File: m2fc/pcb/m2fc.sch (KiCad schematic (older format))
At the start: 31 parts

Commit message: rename m2d to m2fc which now incorporates m2p
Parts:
- added C?: 100n, 0603, symbol C
- added U?: MICROSD, symbol MICROSD
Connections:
- net labels added: SD_CD, SD_CLK, SD_CMD, SD_DAT0, SD_DAT1, SD_DAT2, SD_DAT3
- wire segments 137 -> 119
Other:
- note added: "MICRO SD CARD"
- note removed: "TODO\n* SD Card\n* Thermocouple layout\n* Spec gain resistor for strain gauges"

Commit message: update more bits on flight computer..
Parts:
- removed C?: 1n, 0603, symbol C
- removed IC?: APU1205-HF-3, symbol APU1205-HF-3
- removed IC?: STM32F415RG, symbol STM32F415RG
- added C? (x3): 100n, 0603, symbol C
- added C?: 1n, 0603, symbol C
- added IC?: STM32F405VGT, symbol STM32F405VGT
- added IC?: ADP3335, MSOP-8, symbol ADP3335
- added TP? (x7): TESTPAD, symbol TESTPAD
- C?: value 100n -> 10n; Farnell 1759037 -> 2112704
- R?: Farnell 2331727 -> 2116678
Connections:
- net labels added: BARO_CS, BARO_MISO, BARO_MOSI, BARO_SCK, GYRO_DRDY, GYRO_SCL, GYRO_SDA, HG_ACCEL_CS, HG_ACCEL_INT1, HG_ACCEL_INT2, HG_ACCEL_MISO, HG_ACCEL_MOSI, HG_ACCEL_SCK, LED_1, LED_2, LED_3, LED_A, LED_C, LG_ACCEL_CS, LG_ACCEL_INT1, LG_ACCEL_INT2, LG_ACCEL_MISO, LG_ACCEL_MOSI, LG_ACCEL_SCK, MAGNO_DRDY, MAGNO_SCL, MAGNO_SDA, PYRO_1_C, PYRO_1_F, PYRO_2_C, PYRO_2_F, SER_IN_1, SER_IN_2, SER_OUT_1, SER_OUT_2, STRAIN_1, STRAIN_2, STRAIN_3, THERMO_1, THERMO_2
- wire segments 119 -> 174
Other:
- note added: "* SHARE HALF BRIDGE?\n* TEMPERATURE COMP?"
- moved on the sheet: C?, R?, TP?, X?

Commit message: everything... wired... up...
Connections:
- net BARO_CS: now also IC?.88 (PD7)
- net BARO_MISO: now also IC?.90 (PB4)
- net BARO_MOSI: now also IC?.91 (PB5)
- net BARO_SCK: now also IC?.89 (PB3)
- net BAT_MON: now also IC?.26 (PA3)
- net GYRO_DRDY: now also IC?.97 (PE0)
- net GYRO_SCL: now also IC?.95 (PB8)
- net GYRO_SDA: now also IC?.96 (PB9)
- net HG_ACCEL_CS: now also IC?.29 (PA4)
- net HG_ACCEL_INT1: now also IC?.33 (PC4)
- net HG_ACCEL_INT2: now also IC?.34 (PC5)
- net HG_ACCEL_MISO: now also IC?.31 (PA6)
- net HG_ACCEL_MOSI: now also IC?.32 (PA7)
- net HG_ACCEL_SCK: now also IC?.30 (PA5)
- net LED_1: now also IC?.1 (PE2)
- net LED_2: now also IC?.2 (PE3)
- net LED_3: now also IC?.3 (PE4)
- net LED_A: now also IC?.4 (PE5)
- net LED_C: now also IC?.5 (PE6)
- net LG_ACCEL_CS: now also IC?.51 (PB12)
- net LG_ACCEL_INT1: now also IC?.55 (PD8)
- net LG_ACCEL_INT2: now also IC?.56 (PD9)
- net LG_ACCEL_MISO: now also IC?.53 (PB14)
- net LG_ACCEL_MOSI: now also IC?.54 (PB15)
- net LG_ACCEL_SCK: now also IC?.52 (PB13)
- net MAGNO_DRDY: now also IC?.46 (PE15)
- net MAGNO_SCL: now also IC?.47 (PB10)
- net MAGNO_SDA: now also IC?.48 (PB11)
- net PYRO_1_C: now also IC?.39 (PE8)
- net PYRO_1_F: now also IC?.38 (PE7)
- net PYRO_2_C: now also IC?.40 (PE9)
- net PYRO_2_F: now also IC?.41 (PE10)
- net SD_CD: now also IC?.82 (PD1)
- net SD_CLK: now also IC?.80 (PC12)
- net SD_CMD: now also IC?.83 (PD2)
- net SD_DAT0: now also IC?.65 (PC8)
- net SD_DAT1: now also IC?.66 (PC9)
- net SD_DAT2: now also IC?.78 (PC10)
- net SD_DAT3: now also IC?.79 (PC11)
- net SER_IN_1: now also IC?.93 (PB7)
- net SER_IN_2: now also IC?.87 (PD6)
- net SER_OUT_1: now also IC?.92 (PB6)
- net SER_OUT_2: now also IC?.86 (PD5)
- net STRAIN_1: now also IC?.23 (PA0)
- net STRAIN_2: now also IC?.24 (PA1)
- net STRAIN_3: now also IC?.25 (PA2)
- net SWCLK: now also IC?.76 (PA14)
- net SWDIO: now also IC?.72 (PA13)
- net THERMO_1: now also IC?.16 (PC1)
- net THERMO_2: now also IC?.17 (PC2)
- net THERMO_3: now reaches IC?.18 (PC3)
- net GYRO_INT1: now reaches IC?.98 (PE1)
- no-connect marks 2 -> 30
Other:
- note removed: "* SHARE HALF BRIDGE?\n* TEMPERATURE COMP?"

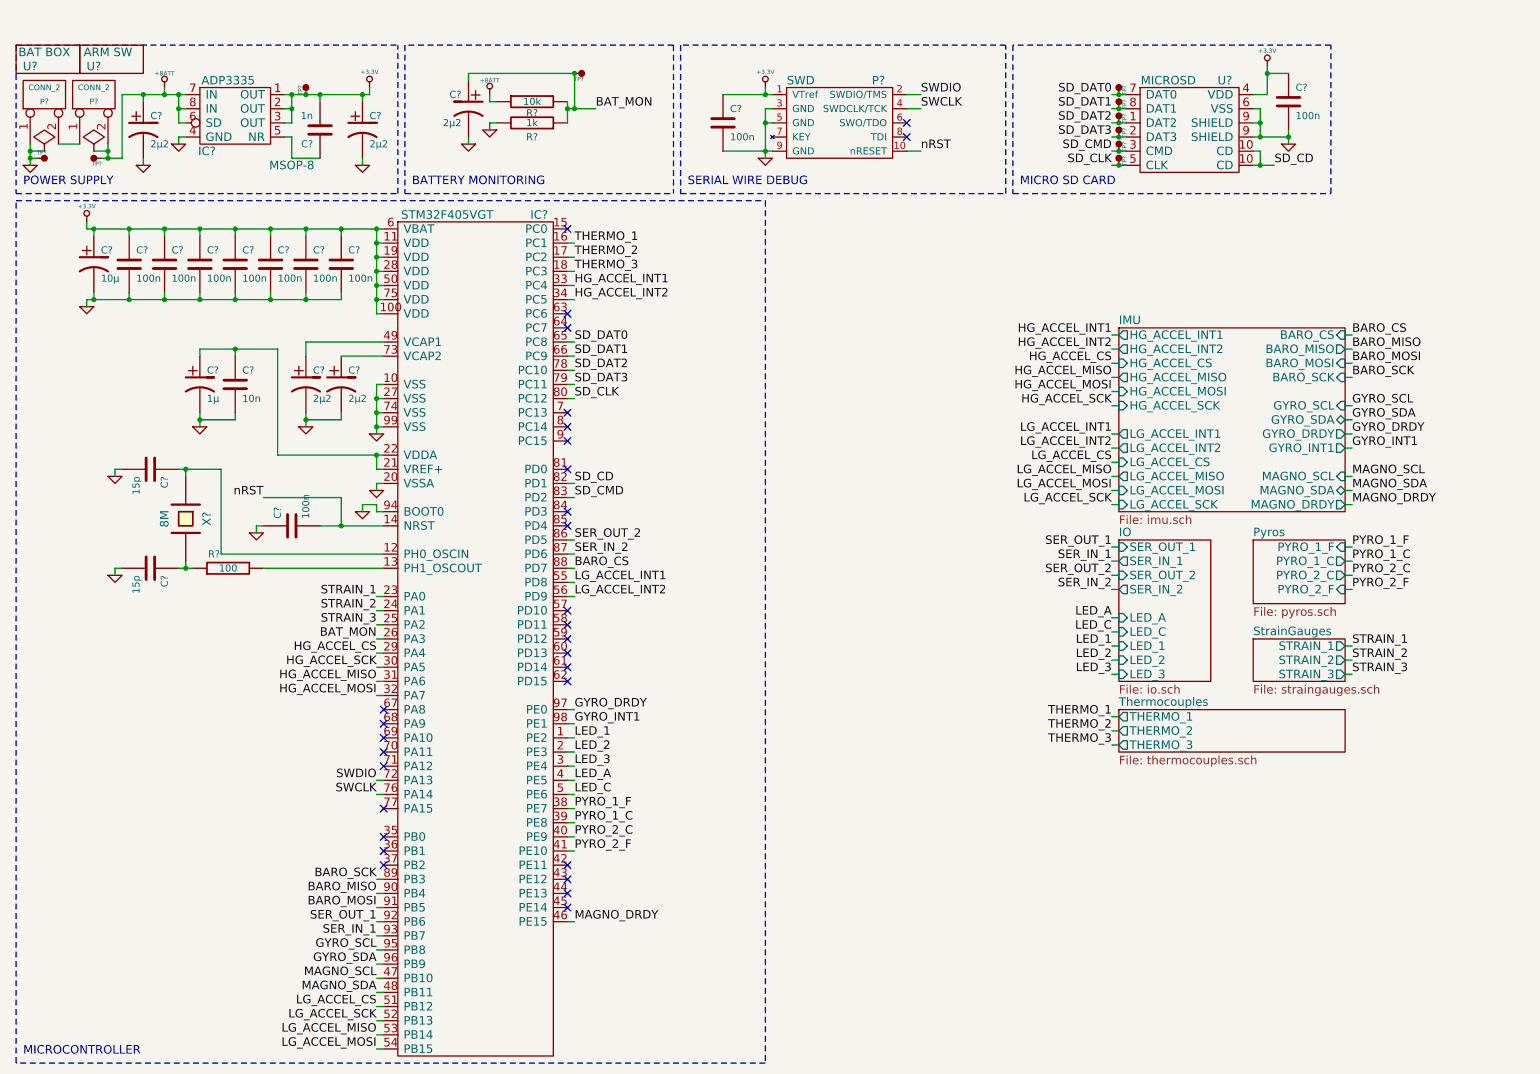
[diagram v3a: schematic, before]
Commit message: fix all the erc errors
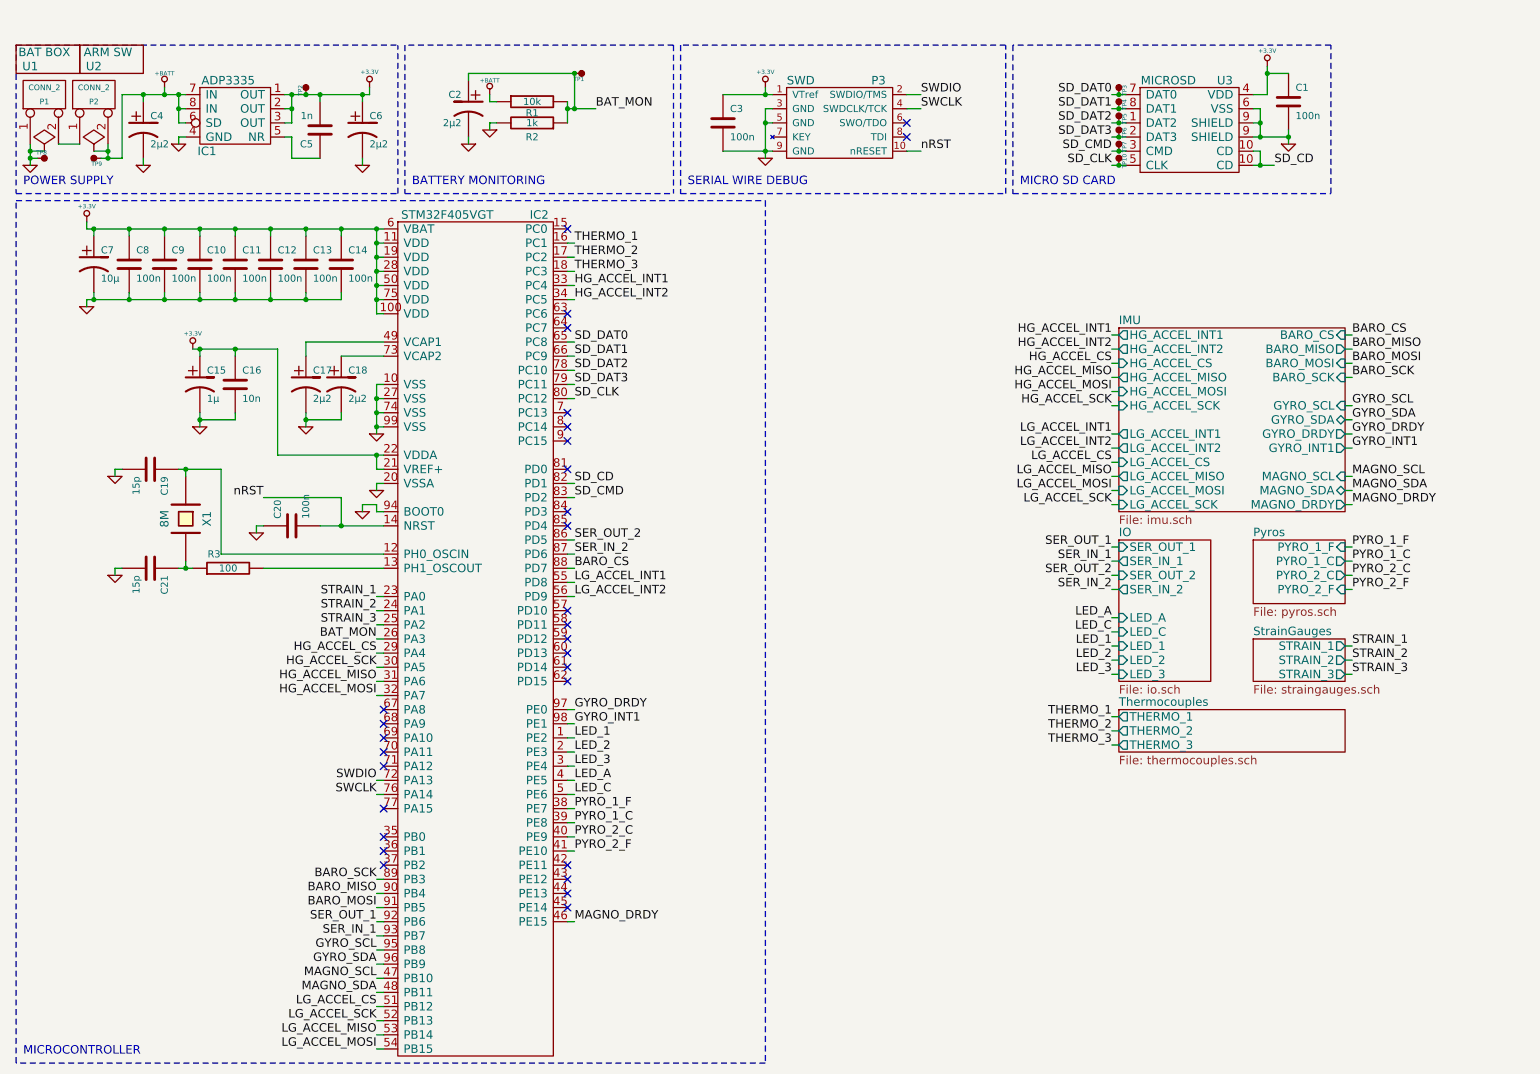
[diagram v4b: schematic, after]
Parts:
- gave numbers to parts that had none: 43
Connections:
- net +3.3V: now also C15.1, C16.1, IC2.21 (VREF+), IC2.22 (VDDA)

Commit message: update m2fc sch with 3rd pyro and SJs
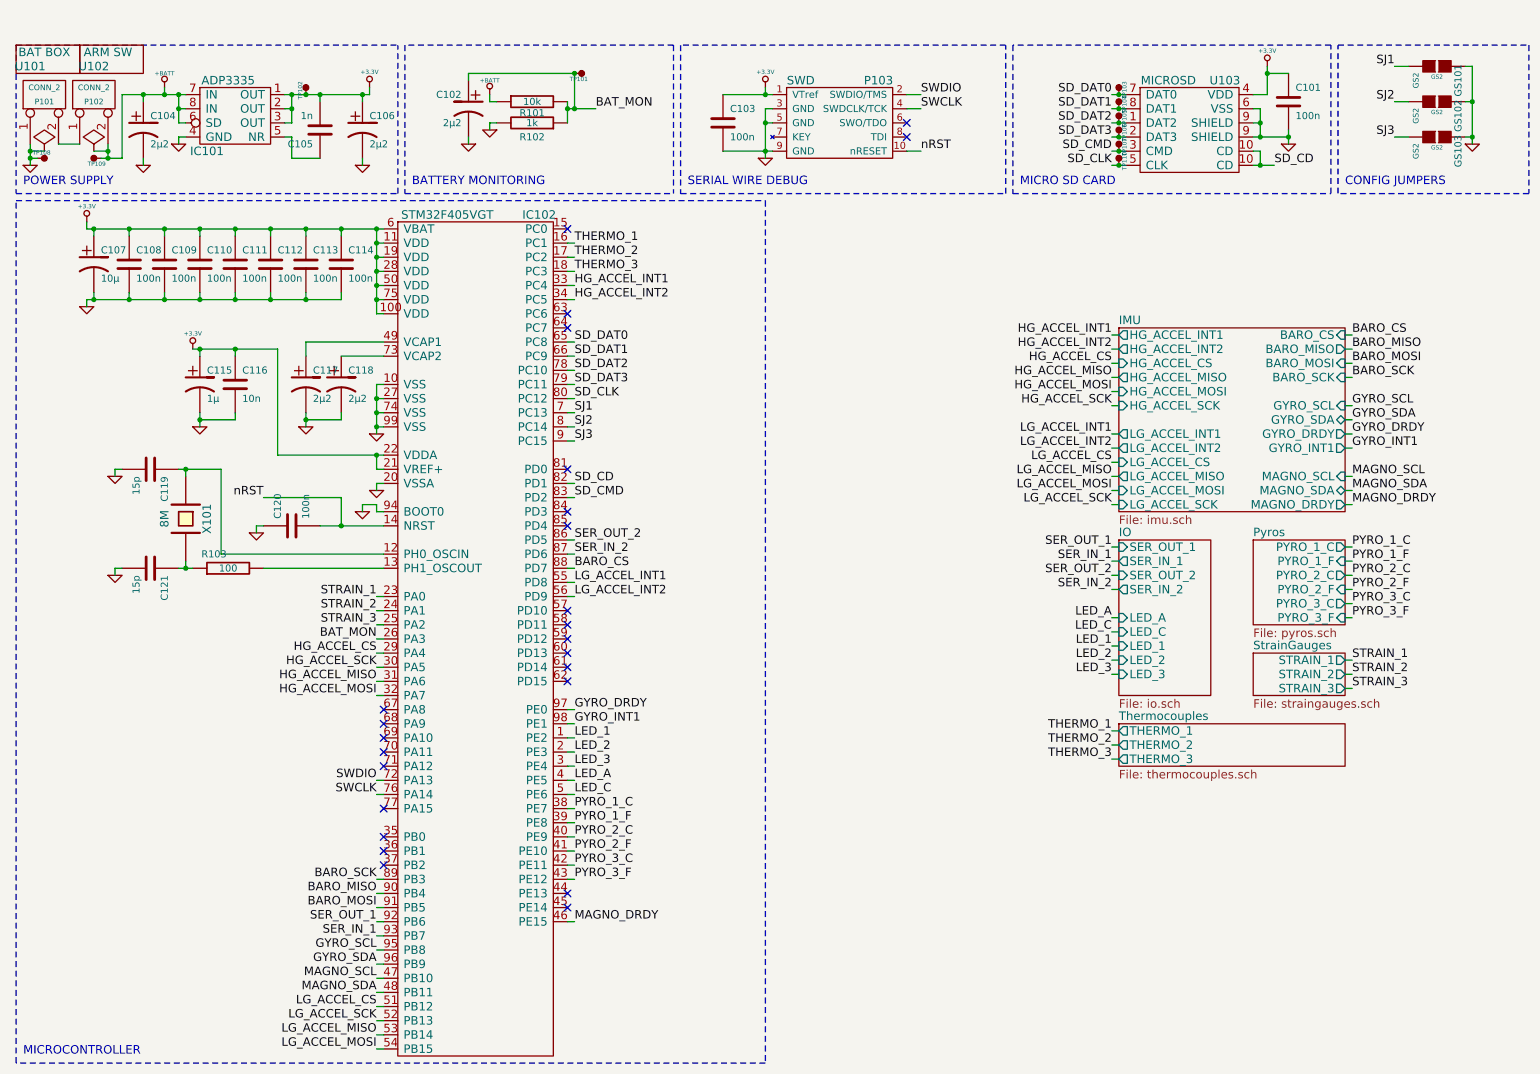
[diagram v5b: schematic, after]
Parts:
- added GS101, GS102, GS103: GS2, GS2, symbol GS2
- renumbered C1 to C101, C2 to C102, C3 to C103, C4 to C104, C5 to C105, C6 to C106, C7 to C107, C8 to C108, C9 to C109, C10 to C110, C11 to C111, C12 to C112, C13 to C113, C14 to C114, C15 to C115, C16 to C116, C17 to C117, C18 to C118, C19 to C119, C20 to C120, C21 to C121, IC1 to IC101, IC2 to IC102, P1 to P101, P2 to P102, P3 to P103, R1 to R101, R2 to R102, R3 to R103, TP1 to TP101, TP2 to TP102, TP3 to TP103, TP4 to TP104, TP5 to TP105, TP6 to TP106, TP7 to TP107, TP8 to TP108, TP9 to TP109, TP10 to TP110, U1 to U101, U2 to U102, U3 to U103, X1 to X101
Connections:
- net GND: now also GS101.1 (G1), GS102.1 (G1), GS103.1 (G1)
- net PYRO_1_C: now also IC102.38 (PE7); no longer IC102.39 (PE8)
- net PYRO_1_F: now also IC102.39 (PE8); no longer IC102.38 (PE7)
- net PYRO_3_C: now reaches IC102.42 (PE11)
- net PYRO_3_F: now reaches IC102.43 (PE12)
- net SJ1: now reaches IC102.7 (PC13)
- net SJ1: now also GS101.2 (G2)
- net SJ2: now reaches IC102.8 (PC14)
- net SJ2: now also GS102.2 (G2)
- net SJ3: now reaches IC102.9 (PC15)
- net SJ3: now also GS103.2 (G2)
- no-connect marks 30 -> 25
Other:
- note added: "CONFIG JUMPERS"

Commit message: swap to JST PA range connectors
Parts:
- added U104, U105: HOUSING, symbol PART
- P101, P102: Farnell 1462926 -> 1830747
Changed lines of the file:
@@
 F 2 "" H 700 850 60  0001 C CNN
 F 3 "" H 700 850 60  0001 C CNN
-F 4 "1462926" V 700 850 60  0001 C CNN "Farnell"
+F 4 "1830747" V 700 850 60  0001 C CNN "Farnell"
 	1    700  850
 	0    -1   -1   0
@@
 F 2 "" H 1050 850 60  0001 C CNN
 F 3 "" H 1050 850 60  0001 C CNN
-F 4 "1462926" V 1050 850 60  0001 C CNN "Farnell"
+F 4 "1830747" V 1050 850 60  0001 C CNN "Farnell"
 	1    1050 850
 	0    -1   -1   0
@@
 F 0 "GS101" H 10650 800 50  0000 C CNN
 F 1 "GS2" H 10650 501 40  0000 C CNN
-F 2 "GS2" V 10624 650 30  0000 C CNN
+F 2 "GS2" V 10624 650 30  0001 C CNN
 F 3 "" H 10550 650 60  0000 C CNN
 	1    10550 650
@@
 F 0 "GS102" H 10650 1050 50  0000 C CNN
 F 1 "GS2" H 10650 751 40  0000 C CNN
-F 2 "GS2" V 10624 900 30  0000 C CNN
+F 2 "GS2" V 10624 900 30  0001 C CNN
 F 3 "" H 10550 900 60  0000 C CNN
 	1    10550 900
@@
 F 0 "GS103" H 10650 1300 50  0000 C CNN
 F 1 "GS2" H 10650 1001 40  0000 C CNN
-F 2 "GS2" V 10624 1150 30  0000 C CNN
+F 2 "GS2" V 10624 1150 30  0001 C CNN
 F 3 "" H 10550 1150 60  0000 C CNN
 	1    10550 1150
@@
 Wire Wire Line
 	4400 3300 4450 3300
+$Comp
+L PART U105
+U 1 1 53CDFCCC
+P 2000 1500
+F 0 "U105" H 2050 1500 60  0000 C CNN
+F 1 "HOUSING" H 2200 1600 60  0000 C CNN
+F 2 "" H 2000 1500 60  0000 C CNN
+F 3 "" H 2000 1500 60  0000 C CNN
+F 4 "1830726" H 2000 1500 60  0001 C CNN "Farnell"
+	1    2000 1500
+	1    0    0    -1
+$EndComp
+$Comp
+L PART U104
+U 1 1 53CDF91F
+P 1550 1500
+F 0 "U104" H 1600 1500 60  0000 C CNN
+F 1 "HOUSING" H 1750 1600 60  0000 C CNN
+F 2 "" H 1550 1500 60  0000 C CNN
+F 3 "" H 1550 1500 60  0000 C CNN
+F 4 "1830726" H 1550 1500 60  0001 C CNN "Farnell"
+	1    1550 1500
+	1    0    0    -1
+$EndComp
 $EndSCHEMATC

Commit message: quick go at wiring diagram
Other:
- note added: "CHECK IF PULLUPS NEEDED"
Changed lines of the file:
@@
 	1    0    0    -1
 $EndComp
+Text Notes 7650 650  0    60   ~ 0
+CHECK IF PULLUPS NEEDED
 $EndSCHEMATC
